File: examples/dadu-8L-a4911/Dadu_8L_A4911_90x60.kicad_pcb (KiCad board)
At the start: 8 copper layers, 90 x 60 mm, 124 parts, among them J1 12V 입력, J2 DAP, J3 CAN, J4 모터 상, J5 홀, J6 UART, Q1 SQD50P04-09L, Q2 IAUC60N04S6N050H, Q3 IAUC60N04S6N050H, Q4 IAUC60N04S6N050H, U1 TPS54331, U2 AMS1117-3.3, U3 LM317, U4 TC364DP, U5 TPS3823-33, U6 TLE9251V, U7 A4911, Y1 20MHz

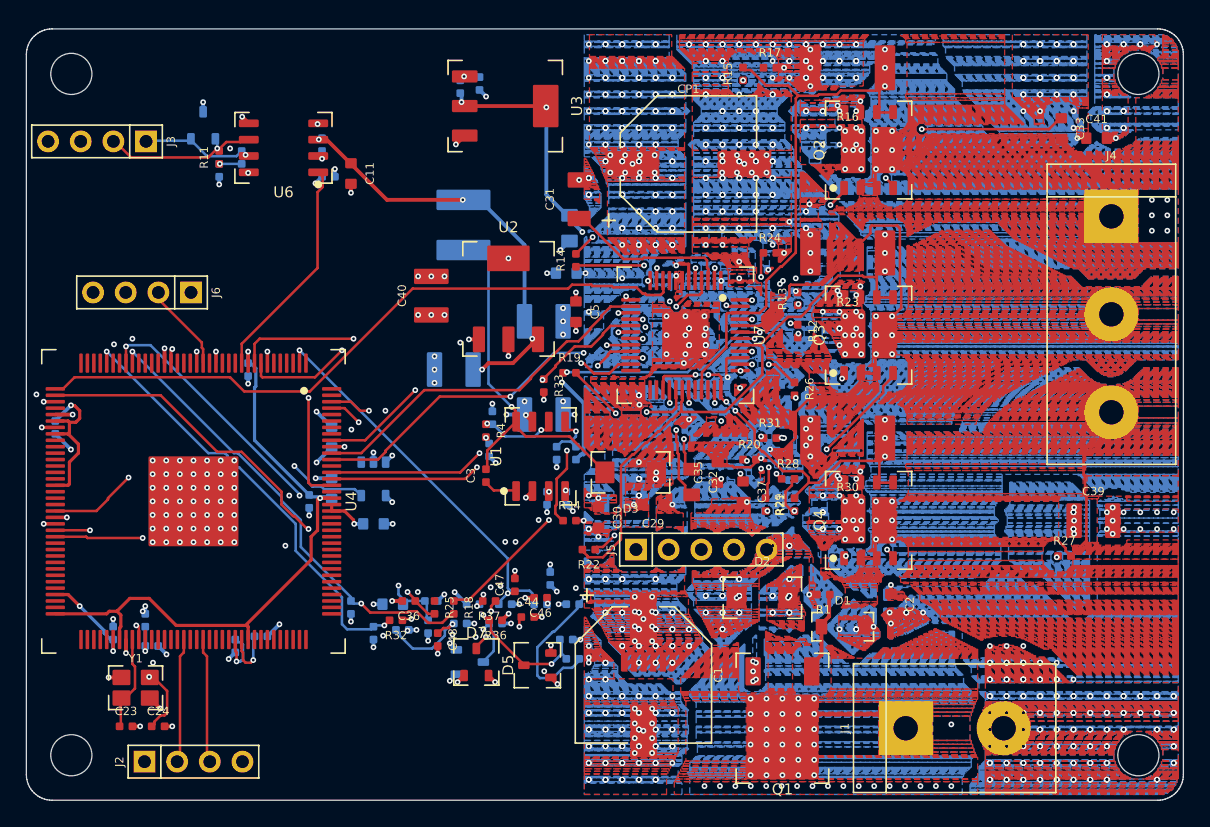
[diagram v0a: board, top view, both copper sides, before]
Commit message: examples: Dadu A4911 8-layer 90x60 updated to seed 47515 (DRC 0, all power widths met, 1 PWM connection by hand)
Co-Authored-By: Claude Opus 5.5 <noreply@anthropic.com>
Claude-Session: https://claude.ai/code/session_01ENBZQtx2ruaEBZiZmBjLaq
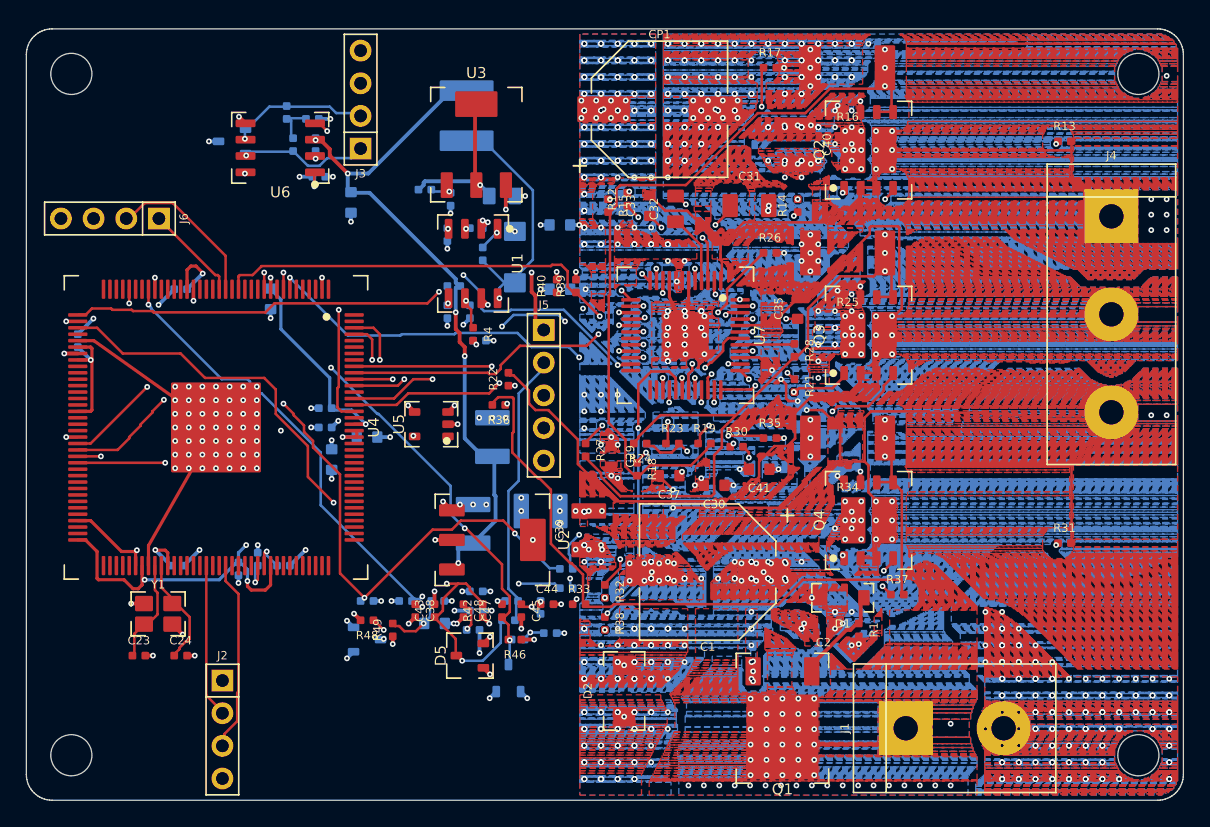
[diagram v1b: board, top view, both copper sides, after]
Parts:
- added R46: 4.7kΩ, pcb_viewer:0402, F.Cu at (63.0, 72.5)
- added R47: 100kΩ, pcb_viewer:0402, B.Cu at (59.8, 71.8)
- added R48: 22kΩ, pcb_viewer:0402, F.Cu at (51.5, 71.0)
- added R49: 10kΩ, pcb_viewer:0402, F.Cu at (53.5, 71.8)
- added U1: TPS54331, pcb_viewer:SOIC-8, F.Cu at (59.8, 43.2)
- added U4: TC364DP, pcb_viewer:TQFP-144, F.Cu at (39.8, 56.0)
- C11, C3, C36, C46, C5, D3, D7, R11: moved to B.Cu
- C38, C43, C45, U5: moved to F.Cu
- R18, R37: value 1kΩ -> 0Ω
- R19, R26, R28: value 10Ω -> 0Ω
- R20, R29: value 10kΩ -> 1kΩ; moved to B.Cu
- R23, R30: value 2mΩ -> 10Ω; footprint pcb_viewer:2512 -> pcb_viewer:0402
- R24, R31: value 0Ω -> 10kΩ
- R25: value 1kΩ -> 2mΩ; footprint pcb_viewer:0402 -> pcb_viewer:2512
- R27: value 10kΩ -> 0Ω
- R32: value 1kΩ -> 10Ω
- R34: value 10kΩ -> 2mΩ; footprint pcb_viewer:0402 -> pcb_viewer:2512
- R35: value 1kΩ -> 0Ω; moved to F.Cu
- R36: value 4.7kΩ -> 0Ω
- R38: value 4.7kΩ -> 1kΩ; moved to F.Cu
- R39: value 1kΩ -> 10kΩ; moved to F.Cu
- R40: value 4.7kΩ -> 10kΩ; moved to F.Cu
- R41: value 100kΩ -> 1kΩ
- R42: value 22kΩ -> 4.7kΩ; moved to F.Cu
- R43: value 10kΩ -> 1kΩ
- R44: renamed from RT1; value NTC 10k -> 4.7kΩ; footprint pcb_viewer:0603 -> pcb_viewer:0402
- R45: renamed from U1; value TPS54331 -> 1kΩ; footprint pcb_viewer:SOIC-8 -> pcb_viewer:0402; moved to B.Cu
- RT1: renamed from U4; value TC364DP -> NTC 10k; footprint pcb_viewer:TQFP-144 -> pcb_viewer:0603; moved to B.Cu
- moved R25 42.3 mm to (88.9, 42.4), turned to 180 degrees
- moved C39 39.3 mm to (68.8, 64.0), turned to 90 degrees
- moved R27 38.2 mm to (68.5, 57.8), turned to 270 degrees
- moved C41 36.8 mm to (82.0, 59.2), turned to 180 degrees
- moved C33 32.6 mm to (73.5, 38.8), turned to 90 degrees
- moved R37 31.8 mm to (92.8, 69.0), turned to 0 degrees
- moved C40 30.8 mm to (85.0, 34.0), turned to 270 degrees
- moved C16 27.3 mm to (37.0, 45.2), turned to 0 degrees
- moved R40 25.1 mm to (66.2, 45.0), turned to 90 degrees
- moved R39 24.9 mm to (67.8, 45.0), turned to 90 degrees
- moved R31 24.3 mm to (105.8, 65.0)
- moved R13 24.1 mm to (105.8, 33.8), turned to 0 degrees
- moved R35 23.0 mm to (82.8, 56.8)
- moved R34 22.6 mm to (88.9, 56.8), turned to 180 degrees
- moved C8 22.5 mm to (57.8, 41.0)
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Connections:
- R18 pad 1: PH_ISNS_U_AMP -> PH_U_SNSP
- R18 pad 2: PH_ISNS_U -> PH_U_SNS
- R19 pad 1: PH_V_HO -> PH_U_LSS
- R19 pad 2: PH_V_HG -> PH_U_SNS
- R20 pad 1: PH_V_HG -> PH_ISNS_U_AMP
- R20 pad 2: PH_V -> PH_ISNS_U
- R21 pad 1: PH_V_LO -> PH_V_HO
- R21 pad 2: PH_V_LG -> PH_V_HG
- R22 pad 1: PH_V_LG -> PH_V_HG
- R22 pad 2: PH_V_SNS -> PH_V
- R23 pad 1: PH_V_SNS -> PH_V_LO
- R23 pad 2: GND -> PH_V_LG
- R24 pad 1: PH_V_SNSM -> PH_V_LG
- R24 pad 2: GND -> PH_V_SNS
- R25 pad 1: PH_ISNS_V_AMP -> PH_V_SNS
- R25 pad 2: PH_ISNS_V -> GND
- R26 pad 1: PH_W_HO -> PH_V_SNSM
- R26 pad 2: PH_W_HG -> GND
- R27 pad 1: PH_W_HG -> PH_V_SNSP
- R27 pad 2: PH_W -> PH_V_SNS
- R28 pad 1: PH_W_LO -> PH_V_LSS
- R28 pad 2: PH_W_LG -> PH_V_SNS
- R29 pad 1: PH_W_LG -> PH_ISNS_V_AMP
- R29 pad 2: PH_W_SNS -> PH_ISNS_V
- R30 pad 1: PH_W_SNS -> PH_W_HO
- R30 pad 2: GND -> PH_W_HG
- R31 pad 1: PH_W_SNSM -> PH_W_HG
- R31 pad 2: GND -> PH_W
- R32 pad 1: PH_ISNS_W_AMP -> PH_W_LO
- R32 pad 2: PH_ISNS_W -> PH_W_LG
- R33 pad 1: PH_DIAG -> PH_W_LG
- R33 pad 2: +3V3 -> PH_W_SNS
- R34 pad 1: PH_EN -> PH_W_SNS
- R35 pad 1: PH_HALL_A_IN -> PH_W_SNSM
- R35 pad 2: PH_HALL_A -> GND
- R36 pad 1: +3V3 -> PH_W_SNSP
- R36 pad 2: PH_HALL_A -> PH_W_SNS
- R37 pad 1: PH_HALL_B_IN -> PH_W_LSS
- R37 pad 2: PH_HALL_B -> PH_W_SNS
- R38 pad 1: +3V3 -> PH_ISNS_W_AMP
- R38 pad 2: PH_HALL_B -> PH_ISNS_W
- R39 pad 1: PH_HALL_C_IN -> PH_DIAG
- R39 pad 2: PH_HALL_C -> +3V3
- R40 pad 1: +3V3 -> PH_EN
- R40 pad 2: PH_HALL_C -> GND
- R41 pad 1: +12V -> PH_HALL_A_IN
- R41 pad 2: VMON -> PH_HALL_A
- R42 pad 1: VMON -> +3V3
- R42 pad 2: GND -> PH_HALL_A
- R43 pad 1: +3V3 -> PH_HALL_B_IN
- R43 pad 2: TEMP -> PH_HALL_B
- R44 pad 1: TEMP -> +3V3
- R44 pad 2: GND -> PH_HALL_B
- R45 pad 1: BUCK_BOOT -> PH_HALL_C_IN
- R45 pad 2: +12V -> PH_HALL_C
- RT1 pad 1: (no net) -> TEMP
- RT1 pad 2: PH_HALL_C -> GND
- U7 pad 27: PH_W_SNS -> PH_W_SNSP
- U7 pad 30: PH_V_SNS -> PH_V_SNSP
- U7 pad 33: PH_U_SNS -> PH_U_SNSP
- U7 pad 36: PH_W_SNS -> PH_W_LSS
- U7 pad 41: PH_V_SNS -> PH_V_LSS
- U7 pad 46: PH_U_SNS -> PH_U_LSS
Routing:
- net PH_INL_U: track 34.4 -> 0.00 mm, vias 2 -> 0
- net PH_W_SNS: track 30.3 -> 59.9 mm, vias 7 -> 3
- net GND: track 47.0 -> 75.8 mm, vias 634 -> 518
- net PH_U_SNSM: track 0.00 -> 27.0 mm, vias 0 -> 2
- net PH_W_LSS: track 0.00 -> 23.6 mm, vias 0 -> 2
- net +9V: track 49.8 -> 26.2 mm, vias 4 -> 2
- net PH_U_VB: track 32.8 -> 9.50 mm
- net PH_U_HG: track 13.2 -> 35.6 mm
- net PH_ISNS_V_AMP: track 0.00 -> 22.1 mm, vias 0 -> 2
- net PH_V: track 64.3 -> 85.7 mm, vias 8 -> 6
- net PH_W: track 57.3 -> 76.3 mm, vias 8 -> 14
- net PH_ISNS_W: track 35.0 -> 53.4 mm, vias 2 -> 4
- net PH_EN: track 70.2 -> 52.5 mm
- net PH_U_SNS: track 44.0 -> 60.6 mm
- net PH_ISNS_U: track 36.5 -> 52.4 mm, vias 2 -> 4
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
